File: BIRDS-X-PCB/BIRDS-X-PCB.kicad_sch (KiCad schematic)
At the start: 6 parts, among them J101 LPC-50M2LG, J102 Conn_02x04_Odd_Even

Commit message: Finish layout
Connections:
- net PROG_DBG_1 renamed ST_SWDIO
- net PROG_DBG_2 renamed ST_SWDCLK
- net PROG_DBG_3 renamed ST_RST
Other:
- note added: "3-Pin Programming via Main Header: 1 - PROG_DBG_1 -> ST_SWDIO 2 - PROG_DBG_2 -> ST_SWDCLK 3 - PROG_DBG_3 -> ST_RST"
- note added: "Select one of these on Digikey NRPN252PARN-RC or LPC-50M2LG (2mm pitch)"
- note removed: "TODO figure out the programming header situation here"
- note removed: "TODO select one of these on Digikey NRPN252PARN-RC or LPC-50M2LG (2mm pitch)"
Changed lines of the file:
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@@
     (effects (font (size 1.27 1.27)) (justify left bottom))
   )
-  (text "TODO select one of these on Digikey\nNRPN252PARN-RC or LPC-50M2LG (2mm pitch)"
+  (text "Select one of these on Digikey\nNRPN252PARN-RC or LPC-50M2LG (2mm pitch)"
     (at 171.45 156.21 0)
     (effects (font (size 1.27 1.27)) (justify left bottom))
@@
     (effects (font (size 1.27 1.27)) (justify left bottom))
   )
-  (text "TODO figure out the programming header situation here"
-    (at 200.66 93.98 0)
+  (text "3-Pin Programming via Main Header:\n  1 - PROG_DBG_1 -> ST_SWDIO\n  2 - PROG_DBG_2 -> ST_SWDCLK\n  3 - PROG_DBG_3 -> ST_RST"
+    (at 218.44 93.98 0)
     (effects (font (size 1.27 1.27)) (justify left bottom))
   )
@@
     (effects (font (size 1.27 1.27)) (justify right))
     (property "Intersheetrefs" "${INTERSHEET_REFS}" (at 155.6024 29.21 0)
+      (effects (font (size 1.27 1.27)) (justify right) hide)
+    )
+  )
+  (global_label "ST_SWDCLK" (shape input) (at 175.26 87.63 180) (fields_autoplaced)
+    (effects (font (size 1.27 1.27)) (justify right))
+    (property "Intersheetrefs" "${INTERSHEET_REFS}" (at 161.7105 87.63 0)
       (effects (font (size 1.27 1.27)) (justify right) hide)
     )
@@
     (effects (font (size 1.27 1.27)) (justify right))
     (property "Intersheetrefs" "${INTERSHEET_REFS}" (at 155.6024 34.29 0)
-      (effects (font (size 1.27 1.27)) (justify right) hide)
-    )
-  )
-  (global_label "PROG_DBG_3" (shape input) (at 201.93 90.17 0) (fields_autoplaced)
-    (effects (font (size 1.27 1.27)) (justify left))
-    (property "Intersheetrefs" "${INTERSHEET_REFS}" (at 216.931 90.17 0)
-      (effects (font (size 1.27 1.27)) (justify left) hide)
-    )
-  )
-  (global_label "PROG_DBG_1" (shape input) (at 201.93 87.63 0) (fields_autoplaced)
-    (effects (font (size 1.27 1.27)) (justify left))
-    (property "Intersheetrefs" "${INTERSHEET_REFS}" (at 216.931 87.63 0)
-      (effects (font (size 1.27 1.27)) (justify left) hide)
-    )
-  )
-  (global_label "PROG_DBG_2" (shape input) (at 175.26 87.63 180) (fields_autoplaced)
-    (effects (font (size 1.27 1.27)) (justify right))
-    (property "Intersheetrefs" "${INTERSHEET_REFS}" (at 160.259 87.63 0)
       (effects (font (size 1.27 1.27)) (justify right) hide)
     )
@@
     )
   )
+  (global_label "ST_SWDIO" (shape input) (at 201.93 87.63 0) (fields_autoplaced)
+    (effects (font (size 1.27 1.27)) (justify left))
+    (property "Intersheetrefs" "${INTERSHEET_REFS}" (at 213.8467 87.63 0)
+      (effects (font (size 1.27 1.27)) (justify left) hide)
+    )
+  )
   (global_label "UART_RX_BOSS_TO_JASPER" (shape input) (at 201.93 107.95 0) (fields_autoplaced)
     (effects (font (size 1.27 1.27)) (justify left))
@@
     )
   )
+  (global_label "ST_RST" (shape input) (at 201.93 90.17 0) (fields_autoplaced)
+    (effects (font (size 1.27 1.27)) (justify left))
+    (property "Intersheetrefs" "${INTERSHEET_REFS}" (at 211.4276 90.17 0)
+      (effects (font (size 1.27 1.27)) (justify left) hide)
+    )
+  )

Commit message: Update resistor vals, plot, BOM
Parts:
- J102: footprint Connector_PinSocket_2.54mm:PinSocket_2x04_P2.54mm_Vertical -> Connector_PinHeader_2.54mm:PinHeader_2x04_P2.54mm_Vertical
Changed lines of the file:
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@@
       (effects (font (size 1.27 1.27)) hide)
     )
-    (property "Footprint" "Connector_PinSocket_2.54mm:PinSocket_2x04_P2.54mm_Vertical" (at 175.26 29.21 0)
+    (property "Footprint" "Connector_PinHeader_2.54mm:PinHeader_2x04_P2.54mm_Vertical" (at 175.26 29.21 0)
       (effects (font (size 1.27 1.27)) hide)
     )

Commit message: RF System updated
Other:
- added sheet RF_System (RF_System.kicad_sch)
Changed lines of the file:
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@@
+    )
+  )
+  (sheet (at 36.83 101.6) (size 31.75 25.4) (fields_autoplaced)
+    (stroke (width 0.1524) (type solid))
+    (fill (color 0 0 0 0.0000))
+    (property "Sheetname" "RF_System" (at 36.83 100.8884 0)
+      (effects (font (size 1.27 1.27)) (justify left bottom))
+    )
+    (property "Sheetfile" "RF_System.kicad_sch" (at 36.83 127.5846 0)
+      (effects (font (size 1.27 1.27)) (justify left top))
+    )
+    (instances
+      (project "BIRDS-X-PCB"
+        (path "/c2796b15-795a-4d6e-ad4b-0ba87ded4bc9" (page "5"))
+      )
     )
   )

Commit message: Rename Experiment to RadfetExperiment
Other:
- sheet Experiment renamed RadfetExperiment
- sheet RadfetExperiment: file Experiment.kicad_sch -> RadfetExperiment.kicad_sch
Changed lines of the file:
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@@
     (stroke (width 0.1524) (type solid))
     (fill (color 0 0 0 0.0000))
-    (property "Sheetname" "Experiment" (at 90.17 23.4184 0)
+    (property "Sheetname" "RadfetExperiment" (at 90.17 23.4184 0)
       (effects (font (size 1.27 1.27)) (justify left bottom))
     )
-    (property "Sheetfile" "Experiment.kicad_sch" (at 90.17 43.7646 0)
+    (property "Sheetfile" "RadfetExperiment.kicad_sch" (at 90.17 43.7646 0)
       (effects (font (size 1.27 1.27)) (justify left top))
     )

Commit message: Add PIN Diode experiment
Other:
- added sheet PINDiodeExperiment (PINDiodeExperiment.kicad_sch)
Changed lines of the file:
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@@
+    )
+  )
+  (sheet (at 90.17 54.61) (size 27.94 17.78) (fields_autoplaced)
+    (stroke (width 0.1524) (type solid))
+    (fill (color 0 0 0 0.0000))
+    (property "Sheetname" "PINDiodeExperiment" (at 90.17 53.8984 0)
+      (effects (font (size 1.27 1.27)) (justify left bottom))
+    )
+    (property "Sheetfile" "PINDiodeExperiment.kicad_sch" (at 90.17 72.9746 0)
+      (effects (font (size 1.27 1.27)) (justify left top))
+    )
+    (instances
+      (project "BIRDS-X-PCB"
+        (path "/c2796b15-795a-4d6e-ad4b-0ba87ded4bc9" (page "6"))
+      )
     )
   )

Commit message: Update footprint assignments
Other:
- sheet PINDiodeExperiment ports: added PIN_OUT_1, PIN_OUT_2, PIN_OUT_3, PIN_OUT_4; removed none
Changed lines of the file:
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@@
       (effects (font (size 1.27 1.27)) (justify left top))
+    )
+    (pin "PIN_OUT_4" output (at 118.11 67.31 0)
+      (effects (font (size 1.27 1.27)) (justify right))
+    )
+    (pin "PIN_OUT_2" output (at 118.11 62.23 0)
+      (effects (font (size 1.27 1.27)) (justify right))
+    )
+    (pin "PIN_OUT_3" output (at 118.11 64.77 0)
+      (effects (font (size 1.27 1.27)) (justify right))
+    )
+    (pin "PIN_OUT_1" output (at 118.11 59.69 0)
+      (effects (font (size 1.27 1.27)) (justify right))
     )
     (instances

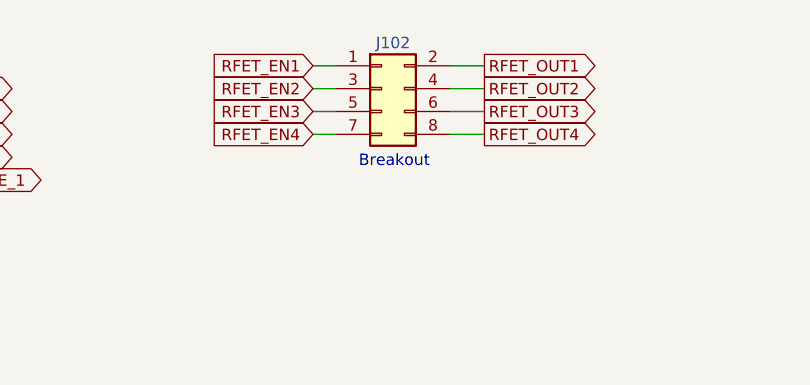
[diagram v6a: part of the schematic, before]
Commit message: Do major layout
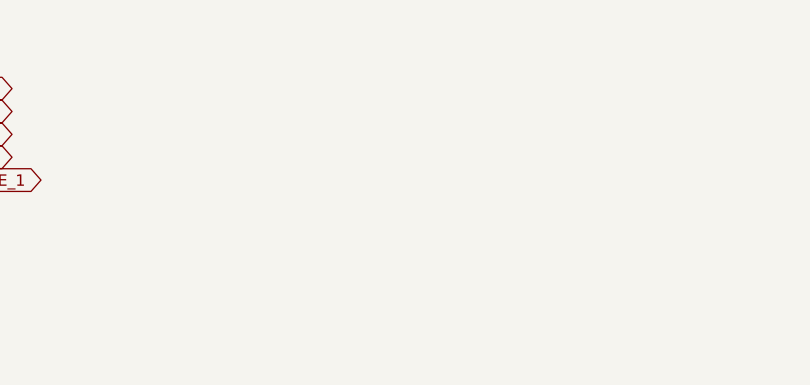
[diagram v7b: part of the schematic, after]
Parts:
- removed J102: Conn_02x04_Odd_Even, Connector_PinHeader_2.54mm:PinHeader_2x04_P2.54mm_Vertical, symbol Connector_Generic:Conn_02x04_Odd_Even
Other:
- note removed: "Breakout"
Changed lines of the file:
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@@
-    (stroke (width 0) (type default))
-  )
-  (wire (pts (xy 167.64 31.75) (xy 170.18 31.75))
     (stroke (width 0) (type default))
   )
@@
     (stroke (width 0) (type default))
   )
-  (wire (pts (xy 167.64 34.29) (xy 170.18 34.29))
-    (stroke (width 0) (type default))
-  )
   (wire (pts (xy 142.24 102.87) (xy 181.61 102.87))
     (stroke (width 0) (type default))
@@
     (stroke (width 0) (type default))
   )
-  (wire (pts (xy 182.88 26.67) (xy 186.69 26.67))
-    (stroke (width 0) (type default))
-  )
   (wire (pts (xy 85.09 29.21) (xy 90.17 29.21))
     (stroke (width 0) (type default))
@@
     (stroke (width 0) (type default))
   )
-  (wire (pts (xy 167.64 26.67) (xy 170.18 26.67))
-    (stroke (width 0) (type default))
-  )
   (wire (pts (xy 175.26 87.63) (xy 181.61 87.63))
     (stroke (width 0) (type default))
   )
-  (wire (pts (xy 182.88 34.29) (xy 186.69 34.29))
-    (stroke (width 0) (type default))
-  )
   (wire (pts (xy 118.11 36.83) (xy 121.92 36.83))
     (stroke (width 0) (type default))
@@
     (stroke (width 0) (type default))
   )
-  (wire (pts (xy 182.88 29.21) (xy 186.69 29.21))
-    (stroke (width 0) (type default))
-  )
   (wire (pts (xy 90.17 31.75) (xy 85.09 31.75))
     (stroke (width 0) (type default))
@@
     (stroke (width 0) (type default))
   )
-  (wire (pts (xy 182.88 31.75) (xy 186.69 31.75))
-    (stroke (width 0) (type default))
-  )
-  (wire (pts (xy 167.64 29.21) (xy 170.18 29.21))
-    (stroke (width 0) (type default))
-  )
   (wire (pts (xy 181.61 115.57) (xy 194.31 115.57))
     (stroke (width 0) (type default))
@@
   (wire (pts (xy 194.31 110.49) (xy 201.93 110.49))
     (stroke (width 0) (type default))
-  )
-  (text "Breakout" (at 172.72 38.1 0)
-    (effects (font (size 1.27 1.27)) (justify left bottom))
   )
   (text "Use SUP_3V3_2 as main power, per ICD" (at 195.58 118.11 0)
@@
     )
   )
-  (global_label "RFET_EN2" (shape input) (at 167.64 29.21 180) (fields_autoplaced)
-    (effects (font (size 1.27 1.27)) (justify right))
-    (property "Intersheetrefs" "${INTERSHEET_REFS}" (at 155.6024 29.21 0)
-      (effects (font (size 1.27 1.27)) (justify right) hide)
-    )
-  )
   (global_label "ST_SWDCLK" (shape input) (at 175.26 87.63 180) (fields_autoplaced)
     (effects (font (size 1.27 1.27)) (justify right))
@@
     )
   )
-  (global_label "RFET_EN4" (shape input) (at 167.64 34.29 180) (fields_autoplaced)
-    (effects (font (size 1.27 1.27)) (justify right))
-    (property "Intersheetrefs" "${INTERSHEET_REFS}" (at 155.6024 34.29 0)
-      (effects (font (size 1.27 1.27)) (justify right) hide)
-    )
-  )
-  (global_label "RFET_OUT4" (shape output) (at 186.69 34.29 0) (fields_autoplaced)
-    (effects (font (size 1.27 1.27)) (justify left))
-    (property "Intersheetrefs" "${INTERSHEET_REFS}" (at 199.8767 34.29 0)
-      (effects (font (size 1.27 1.27)) (justify left) hide)
-    )
-  )
-  (global_label "RFET_EN1" (shape input) (at 167.64 26.67 180) (fields_autoplaced)
-    (effects (font (size 1.27 1.27)) (justify right))
-    (property "Intersheetrefs" "${INTERSHEET_REFS}" (at 155.6024 26.67 0)
-      (effects (font (size 1.27 1.27)) (justify right) hide)
-    )
-  )
   (global_label "SUP_5V0" (shape input) (at 175.26 105.41 180) (fields_autoplaced)
     (effects (font (size 1.27 1.27)) (justify right))
@@
     )
   )
-  (global_label "RFET_OUT1" (shape output) (at 186.69 26.67 0) (fields_autoplaced)
-    (effects (font (size 1.27 1.27)) (justify left))
-    (property "Intersheetrefs" "${INTERSHEET_REFS}" (at 199.8767 26.67 0)
-      (effects (font (size 1.27 1.27)) (justify left) hide)
-    )
-  )
   (global_label "SUP_3V3_1" (shape input) (at 175.26 148.59 180) (fields_autoplaced)
     (effects (font (size 1.27 1.27)) (justify right))
@@
     )
   )
-  (global_label "RFET_OUT2" (shape output) (at 186.69 29.21 0) (fields_autoplaced)
-    (effects (font (size 1.27 1.27)) (justify left))
-    (property "Intersheetrefs" "${INTERSHEET_REFS}" (at 199.8767 29.21 0)
-      (effects (font (size 1.27 1.27)) (justify left) hide)
-    )
-  )
   (global_label "RFET_OUT1" (shape output) (at 121.92 29.21 0) (fields_autoplaced)
     (effects (font (size 1.27 1.27)) (justify left))
@@
     )
   )
-  (global_label "RFET_EN3" (shape input) (at 167.64 31.75 180) (fields_autoplaced)
-    (effects (font (size 1.27 1.27)) (justify right))
-    (property "Intersheetrefs" "${INTERSHEET_REFS}" (at 155.6024 31.75 0)
-      (effects (font (size 1.27 1.27)) (justify right) hide)
-    )
-  )
   (global_label "RFET_EN2" (shape input) (at 85.09 31.75 180) (fields_autoplaced)
     (effects (font (size 1.27 1.27)) (justify right))
@@
     )
   )
-  (global_label "RFET_OUT3" (shape output) (at 186.69 31.75 0) (fields_autoplaced)
-    (effects (font (size 1.27 1.27)) (justify left))
-    (property "Intersheetrefs" "${INTERSHEET_REFS}" (at 199.8767 31.75 0)
-      (effects (font (size 1.27 1.27)) (justify left) hide)
-    )
-  )
-  (symbol (lib_id "Connector_Generic:Conn_02x04_Odd_Even") (at 175.26 29.21 0) (unit 1)
-    (in_bom yes) (on_board yes) (dnp no)
-    (property "Reference" "J102" (at 176.53 24.13 0)
-      (effects (font (size 1.27 1.27)))
-    )
-    (property "Value" "Conn_02x04_Odd_Even" (at 176.53 24.13 0)
-      (effects (font (size 1.27 1.27)) hide)
-    )
-    (property "Footprint" "Connector_PinHeader_2.54mm:PinHeader_2x04_P2.54mm_Vertical" (at 175.26 29.21 0)
-      (effects (font (size 1.27 1.27)) hide)
-    )
-    (property "Datasheet" "~" (at 175.26 29.21 0)
-      (effects (font (size 1.27 1.27)) hide)
-    )
-    (pin "1")
-    (pin "2")
-    (pin "3")
-    (pin "4")
-    (pin "5")
-    (pin "6")
-    (pin "7")
-    (pin "8")
-    (instances
-      (project "BIRDS-X-PCB"
-        (path "/c2796b15-795a-4d6e-ad4b-0ba87ded4bc9"
-          (reference "J102") (unit 1)
-        )
-      )
-    )
-  )

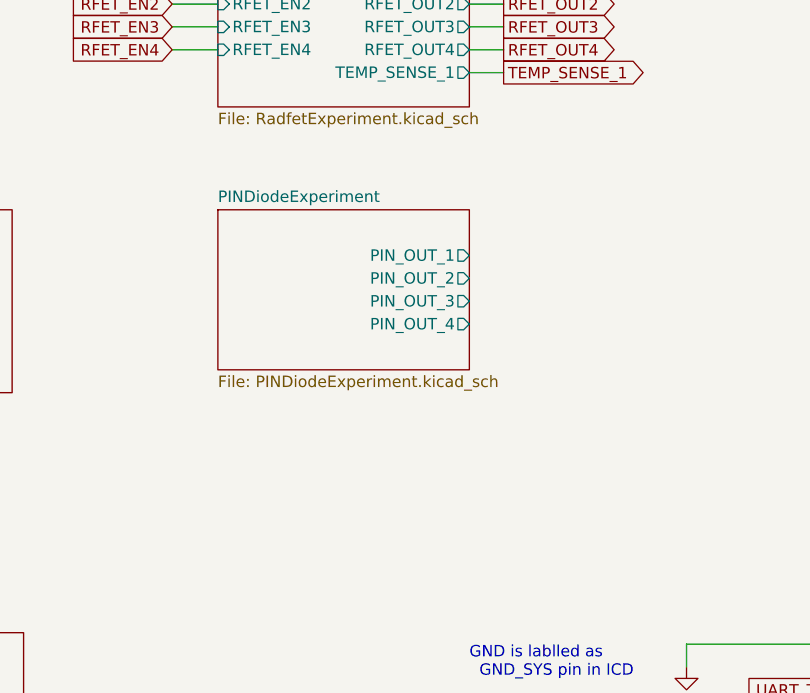
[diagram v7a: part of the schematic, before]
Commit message: Re-organize PIN diode sheet structure
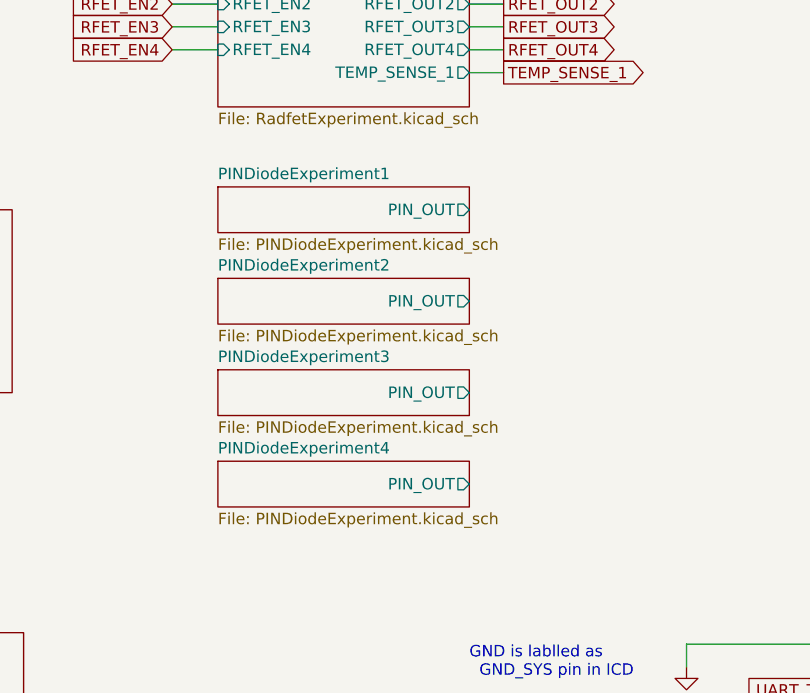
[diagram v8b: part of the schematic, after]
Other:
- sheet PINDiodeExperiment renamed PINDiodeExperiment1
- added sheet PINDiodeExperiment2 (PINDiodeExperiment.kicad_sch)
- added sheet PINDiodeExperiment3 (PINDiodeExperiment.kicad_sch)
- added sheet PINDiodeExperiment4 (PINDiodeExperiment.kicad_sch)
- sheet PINDiodeExperiment1 ports: added PIN_OUT; removed PIN_OUT_1, PIN_OUT_2, PIN_OUT_3, PIN_OUT_4
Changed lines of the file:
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@@
+    )
+  )
+  (sheet (at 90.17 82.55) (size 27.94 5.08) (fields_autoplaced)
+    (stroke (width 0.1524) (type solid))
+    (fill (color 0 0 0 0.0000))
+    (property "Sheetname" "PINDiodeExperiment4" (at 90.17 81.8384 0)
+      (effects (font (size 1.27 1.27)) (justify left bottom))
+    )
+    (property "Sheetfile" "PINDiodeExperiment.kicad_sch" (at 90.17 88.2146 0)
+      (effects (font (size 1.27 1.27)) (justify left top))
+    )
+    (pin "PIN_OUT" output (at 118.11 85.09 0)
+      (effects (font (size 1.27 1.27)) (justify right))
+    )
+    (instances
+      (project "BIRDS-X-PCB"
+        (path "/c2796b15-795a-4d6e-ad4b-0ba87ded4bc9" (page "9"))
+      )
+    )
+  )
+  (sheet (at 90.17 72.39) (size 27.94 5.08) (fields_autoplaced)
+    (stroke (width 0.1524) (type solid))
+    (fill (color 0 0 0 0.0000))
+    (property "Sheetname" "PINDiodeExperiment3" (at 90.17 71.6784 0)
+      (effects (font (size 1.27 1.27)) (justify left bottom))
+    )
+    (property "Sheetfile" "PINDiodeExperiment.kicad_sch" (at 90.17 78.0546 0)
+      (effects (font (size 1.27 1.27)) (justify left top))
+    )
+    (pin "PIN_OUT" output (at 118.11 74.93 0)
+      (effects (font (size 1.27 1.27)) (justify right))
+    )
+    (instances
+      (project "BIRDS-X-PCB"
+        (path "/c2796b15-795a-4d6e-ad4b-0ba87ded4bc9" (page "8"))
+      )
     )
   )
@@
     )
   )
-  (sheet (at 90.17 54.61) (size 27.94 17.78) (fields_autoplaced)
+  (sheet (at 90.17 62.23) (size 27.94 5.08) (fields_autoplaced)
     (stroke (width 0.1524) (type solid))
     (fill (color 0 0 0 0.0000))
-    (property "Sheetname" "PINDiodeExperiment" (at 90.17 53.8984 0)
+    (property "Sheetname" "PINDiodeExperiment2" (at 90.17 61.5184 0)
       (effects (font (size 1.27 1.27)) (justify left bottom))
     )
-    (property "Sheetfile" "PINDiodeExperiment.kicad_sch" (at 90.17 72.9746 0)
+    (property "Sheetfile" "PINDiodeExperiment.kicad_sch" (at 90.17 67.8946 0)
       (effects (font (size 1.27 1.27)) (justify left top))
     )
-    (pin "PIN_OUT_4" output (at 118.11 67.31 0)
+    (pin "PIN_OUT" output (at 118.11 64.77 0)
       (effects (font (size 1.27 1.27)) (justify right))
     )
-    (pin "PIN_OUT_2" output (at 118.11 62.23 0)
+    (instances
+      (project "BIRDS-X-PCB"
+        (path "/c2796b15-795a-4d6e-ad4b-0ba87ded4bc9" (page "7"))
+      )
+    )
+  )
+  (sheet (at 90.17 52.07) (size 27.94 5.08) (fields_autoplaced)
+    (stroke (width 0.1524) (type solid))
+    (fill (color 0 0 0 0.0000))
+    (property "Sheetname" "PINDiodeExperiment1" (at 90.17 51.3584 0)
+      (effects (font (size 1.27 1.27)) (justify left bottom))
+    )
+    (property "Sheetfile" "PINDiodeExperiment.kicad_sch" (at 90.17 57.7346 0)
+      (effects (font (size 1.27 1.27)) (justify left top))
+    )
+    (pin "PIN_OUT" output (at 118.11 54.61 0)
       (effects (font (size 1.27 1.27)) (justify right))
     )
-    (pin "PIN_OUT_3" output (at 118.11 64.77 0)
-      (effects (font (size 1.27 1.27)) (justify right))
-    )
-    (pin "PIN_OUT_1" output (at 118.11 59.69 0)
-      (effects (font (size 1.27 1.27)) (justify right))
-    )
